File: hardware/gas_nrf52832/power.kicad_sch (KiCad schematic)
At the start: 25 parts, among them IC6 NPM1100-QDAA-R, J3 Batt_SW, J5 USB4515-GF-A, Q4 DMC2400UV-7

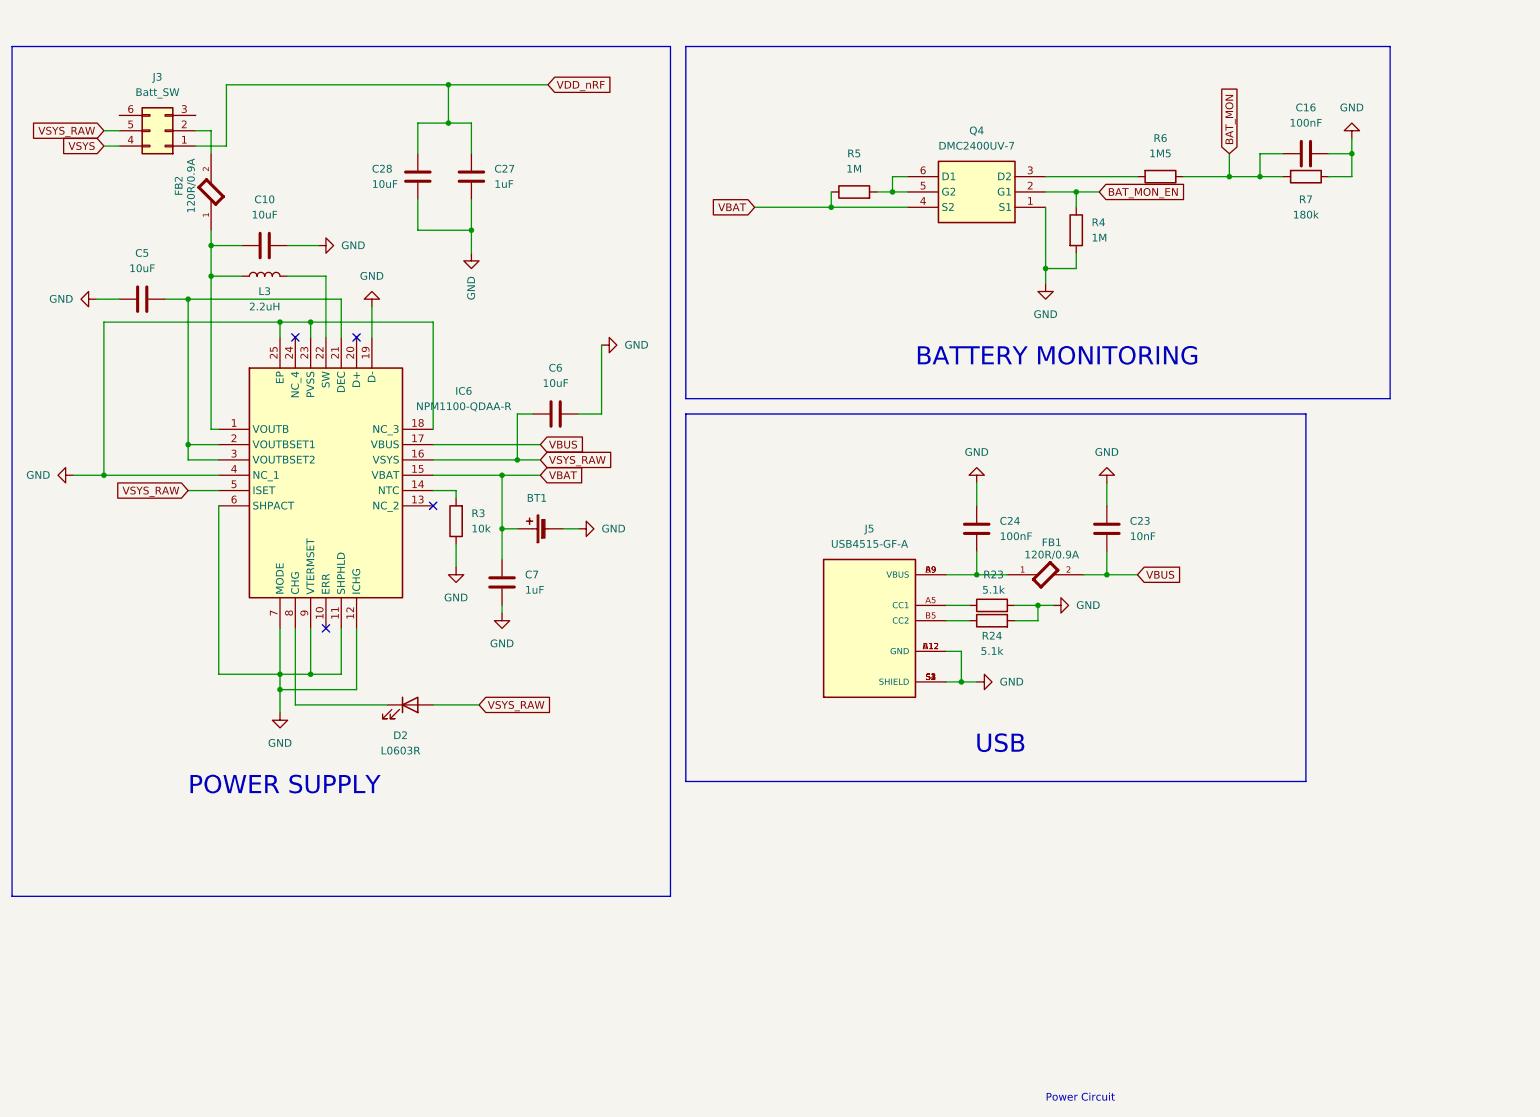
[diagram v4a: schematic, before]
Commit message: feat: hw revision 2.0.1
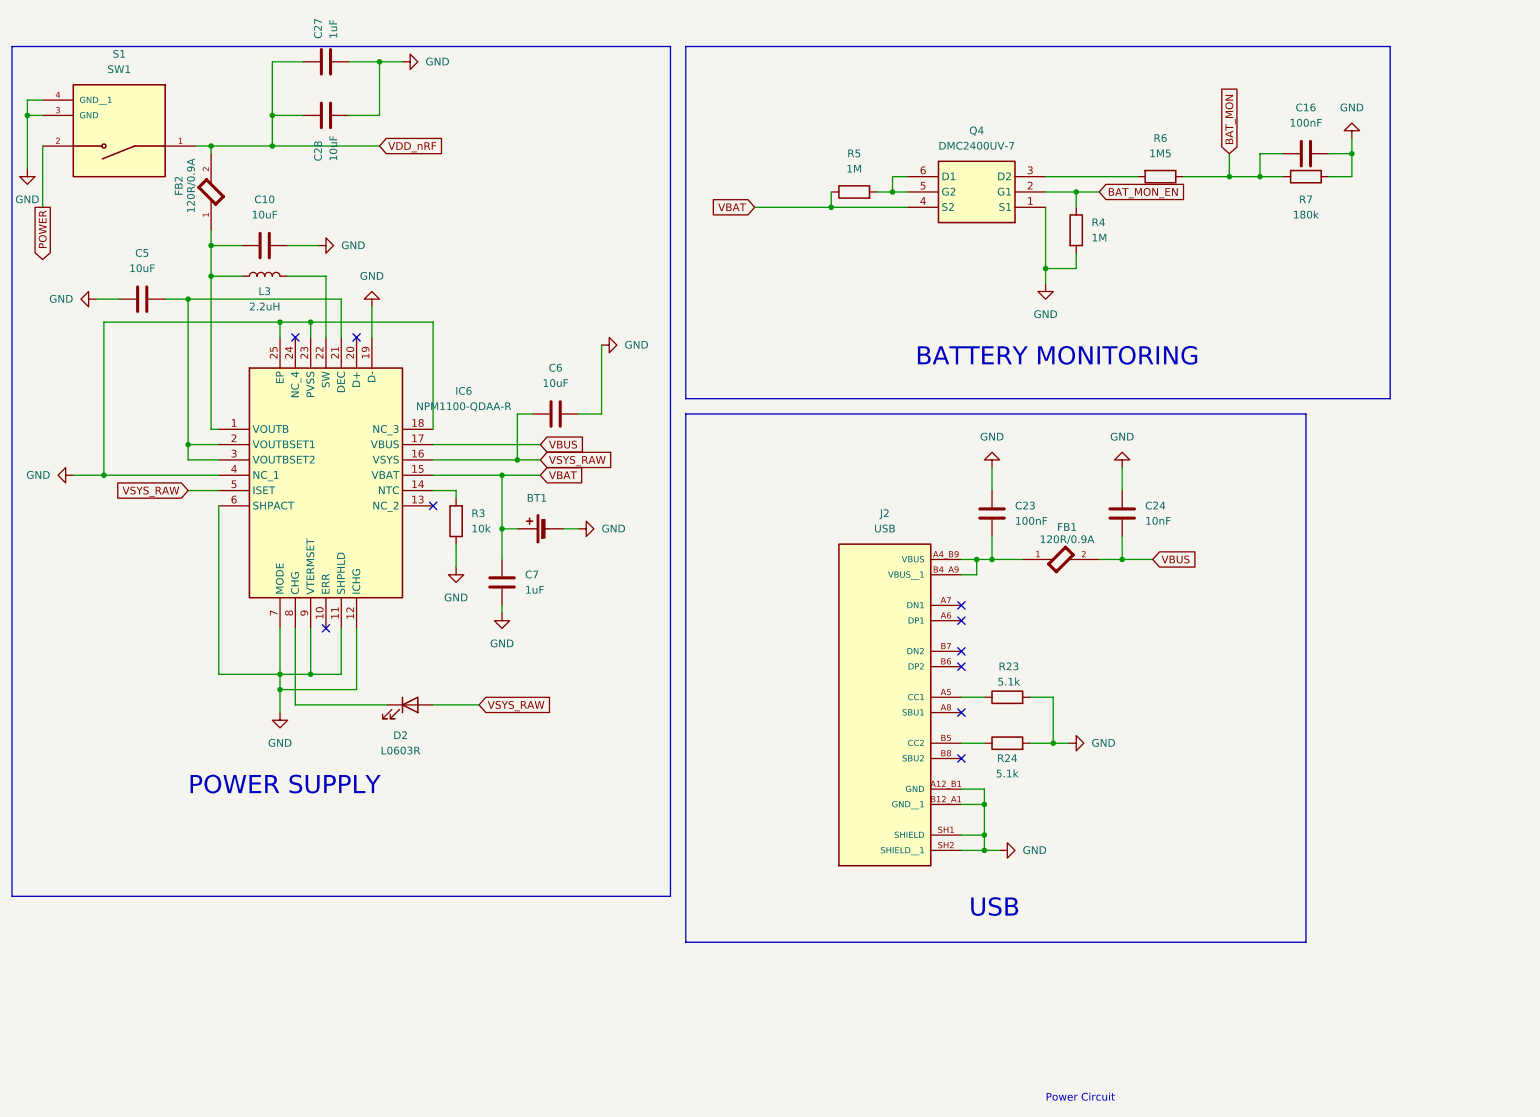
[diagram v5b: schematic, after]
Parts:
- removed J3: Batt_SW, HHS:MSL-1C2P, symbol Connector_Generic:Conn_02x03_Top_Bottom
- removed J5: USB4515-GF-A, USB4515-GF-A_REVA:GCT_USB4515-GF-A_REVA, symbol USB4515-GF-A_REVA:USB4515-GF-A_REVA
- added J2: USB, UJ20-C-G-MSMT-TR-68:CUI_UJ20-C-G-MSMT-TR-68, symbol UJ20-C-G-MSMT-TR-68:UJ20-C-G-MSMT-TR-68
- added S1: SW1, TS11-674-43-BK-100-RA-D:SW_TS11-674-43-BK-100-RA-D, symbol TS11-674-43-BK-100-RA-D:TS11-674-43-BK-100-RA-D
- C23: value 10nF -> 100nF; Manufacturer_Part_Number CL05B103KB5NNNC -> CL05B104KO5NNNC
- C24: value 100nF -> 10nF; Manufacturer_Part_Number CL05B104KO5NNNC -> CL05B103KB5NNNC
- D2: footprint LED_SMD:LED_0603_1608Metric -> WP1533BQ_ID:WP1533BQ; MANUFACTURER BRIGHT LED -> Kingbright; Manufacturer_Part_Number BL-HUF36A-AV-TRB -> WP1533BQ/ID; Package 0603 (1608 Metric) -> Tube; Type Surface Mount -> Through Hole; now left out of the parts list
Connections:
- net GND: now also J2.A12_B1 (GND), J2.B12_A1 (GND__1), J2.SH1 (SHIELD), J2.SH2 (SHIELD__1), S1.3 (GND), S1.4 (GND__1)
- net VBUS: now also C24.2; no longer C23.2
- net VDD_nRF: now also FB2.2, S1.1
- net at R24.1: now also J2.B5 (CC2)
- net at R23.1: now also J2.A5 (CC1)
- net at FB1.1: now also C23.2, J2.A4_B9 (VBUS), J2.B4_A9 (VBUS__1); no longer C24.2
- new net POWER: S1.2
- no-connect marks 4 -> 10
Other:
- moved on the sheet: C27, C28

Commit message: hw 2.0.1 smt add
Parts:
- S1: MANUFACTURER CUI Devices -> SUNGMUN; Manufacturer_Part_Number TS11-674-43-BK-100-RA-D -> STP-1117
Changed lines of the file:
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@@
 			)
 		)
-		(property "Description" "SWITCH TACTILE SPST-NO 0.05A 12V"
+		(property "Description" "SWITCH TACTILE SPST"
 			(at 33.02 29.21 0)
 			(effects
@@
 			)
 		)
-		(property "MANUFACTURER" "CUI Devices"
+		(property "MANUFACTURER" "SUNGMUN"
 			(at 33.02 29.21 0)
 			(effects
@@
 			)
 		)
-		(property "Manufacturer_Part_Number" "TS11-674-43-BK-100-RA-D"
+		(property "Manufacturer_Part_Number" "STP-1117"
 			(at 33.02 29.21 0)
 			(effects
